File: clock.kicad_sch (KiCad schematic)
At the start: 51 parts, among them J1 USB_C_Receptacle_USB2.0_16P, J2 Conn_01x02_Pin, J3 Conn_01x02_Pin, J4 Conn_01x02_Pin, J5 Battery, Q1 2N7002K, Q2 NPN, SW1 SW_Push, SW2 SW_Push, SW3 SW_Push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

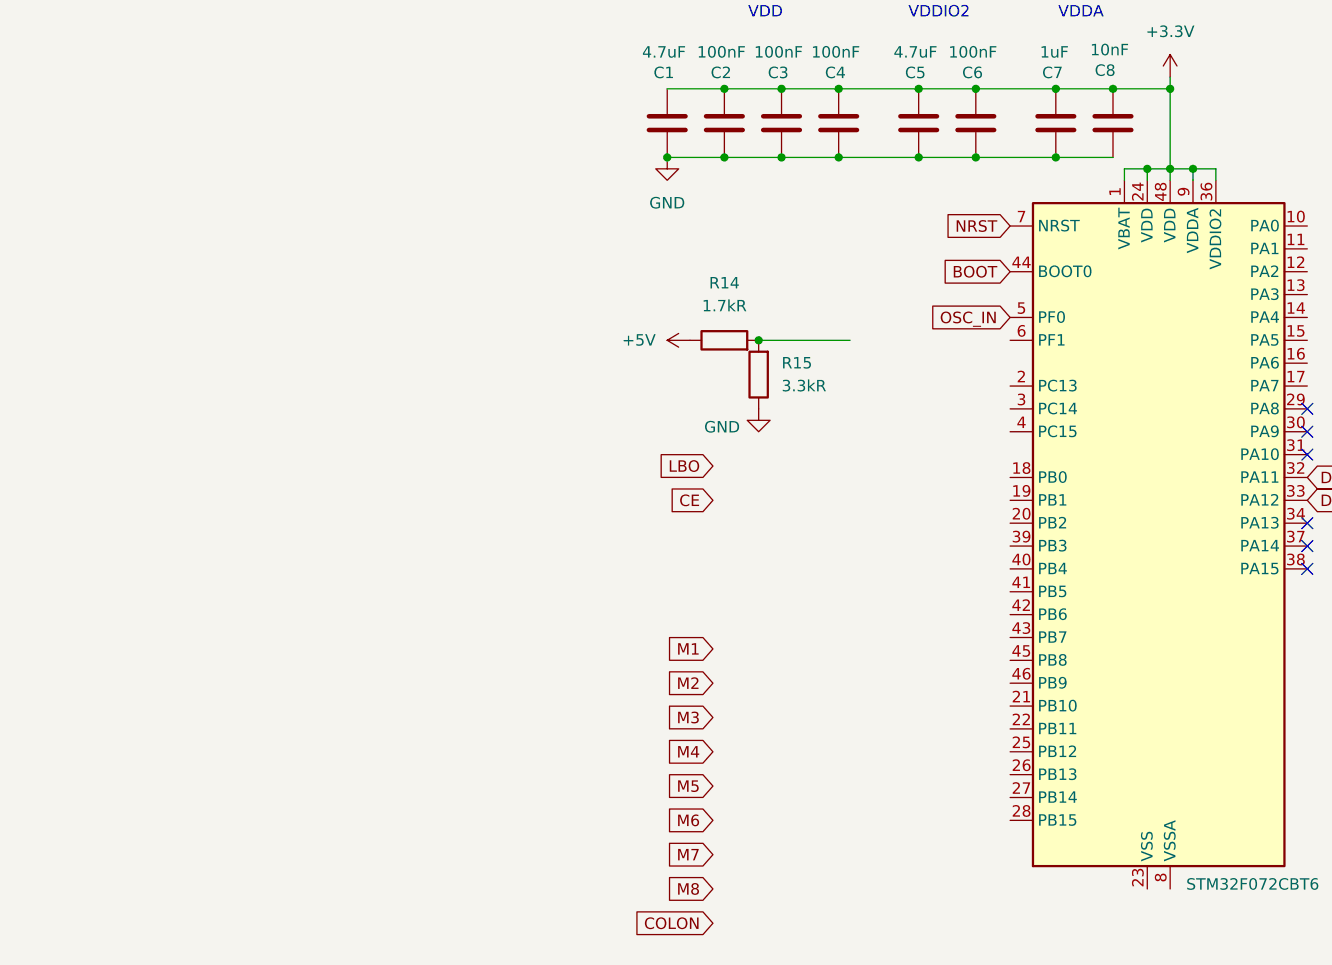
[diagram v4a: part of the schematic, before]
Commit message: actually grounded STM, changed charlie plexed resistors, added note for charging logic, added switch for the 5V logic detection
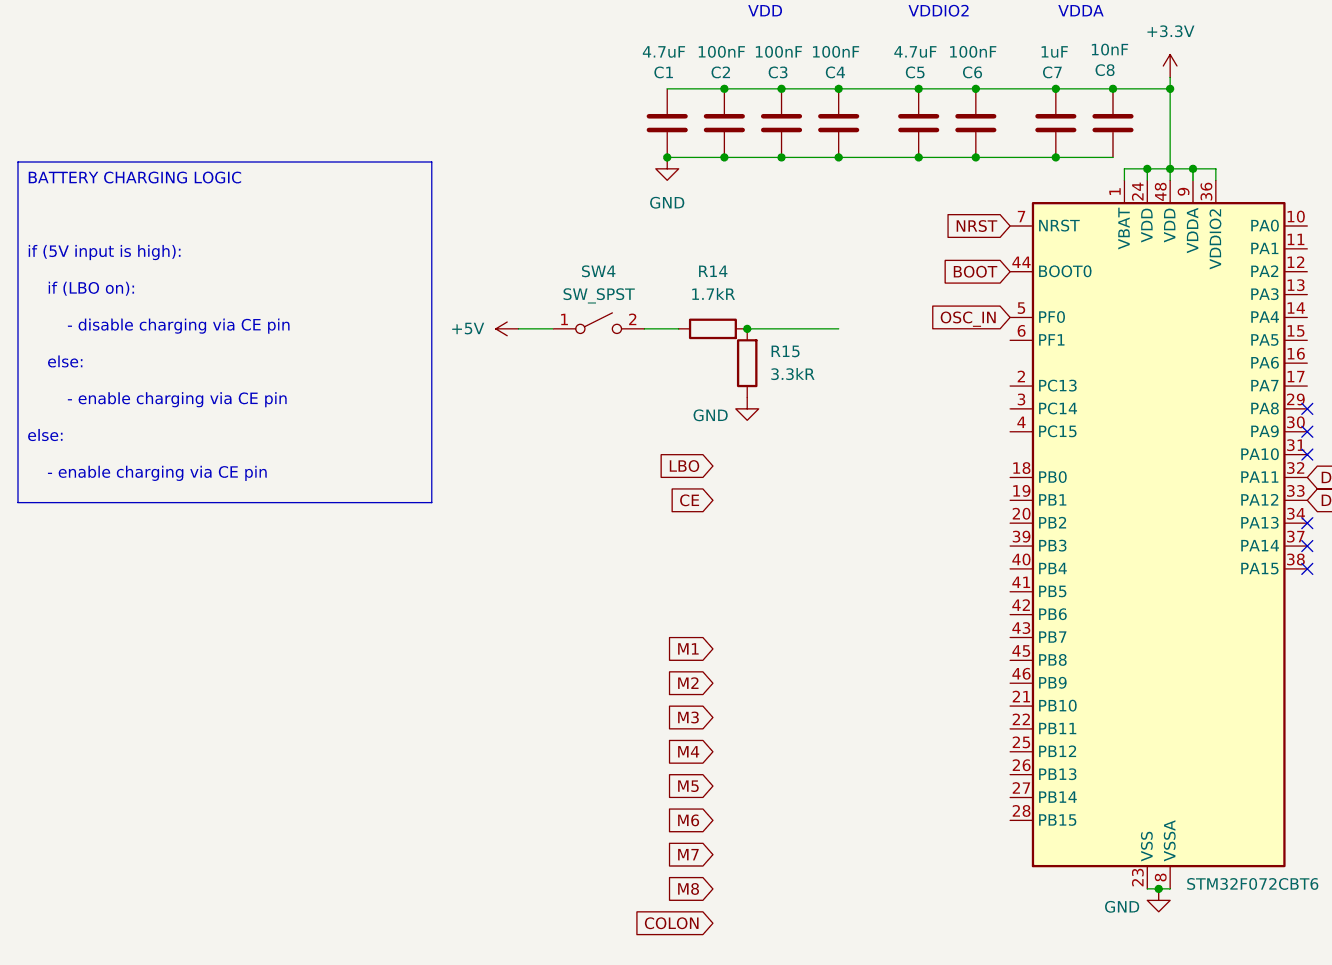
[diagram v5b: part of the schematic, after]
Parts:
- added SW4: SW_SPST, symbol Switch:SW_SPST
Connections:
- net +5V: now also SW4.1 (A); no longer R14.1
- net GND: now also U1.23 (VSS), U1.35 (VSS), U1.47 (VSS), U1.8 (VSSA)
- new net: R14.1, SW4.2 (B)
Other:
- moved on the sheet: R14, R15
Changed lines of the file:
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@@
 	)
 	(junction
+		(at 71.12 189.23)
+		(diameter 0)
+		(color 0 0 0 0)
+	)
+	(junction
 		(at 35.56 107.95)
 		(diameter 0)
@@
 	)
 	(junction
-		(at 26.67 128.27)
+		(at 25.4 127)
 		(diameter 0)
 		(color 0 0 0 0)
@@
 	(wire
 		(pts
-			(xy 26.67 128.27) (xy 36.83 128.27)
+			(xy 25.4 127) (xy 35.56 127)
+		)
+		(stroke
+			(width 0)
+			(type default)
+		)
+	)
+	(wire
+		(pts
+			(xy 71.12 189.23) (xy 72.39 189.23)
 		)
 		(stroke
@@
 	(wire
 		(pts
+			(xy 69.85 189.23) (xy 71.12 189.23)
+		)
+		(stroke
+			(width 0)
+			(type default)
+		)
+	)
+	(wire
+		(pts
+			(xy 3.81 127) (xy 0 127)
+		)
+		(stroke
+			(width 0)
+			(type default)
+		)
+	)
+	(wire
+		(pts
 			(xy 153.67 107.95) (xy 168.91 107.95)
 		)
@@
 	(wire
 		(pts
+			(xy 17.78 127) (xy 13.97 127)
+		)
+		(stroke
+			(width 0)
+			(type default)
+		)
+	)
+	(wire
+		(pts
 			(xy 153.67 90.17) (xy 158.75 90.17)
 		)
@@
 		)
 	)
+	(text_box "BATTERY CHARGING LOGIC\n\n\n\nif (5V input is high):\n\n	if (LBO on):\n		\n		- disable charging via CE pin\n\n	else:\n		\n		- enable charging via CE pin\n\nelse:\n\n	- enable charging via CE pin\n"
+		(exclude_from_sim no)
+		(at -55.626 108.458 0)
+		(size 45.974 37.846)
+		(stroke
+			(width 0)
+			(type default)
+		)
+		(fill
+			(type none)
+		)
+		(effects
+			(font
+				(size 1.27 1.27)
+			)
+			(justify left top)
+		)
+	)
 	(text_box "\"It is recommended to use X7R or X5R dielectric capacitor if 1.0µF ceramic capacitor is selected as input/output capacitors.\""
 		(exclude_from_sim no)
@@
 	(symbol
 		(lib_id "Device:R")
-		(at 22.86 128.27 90)
+		(at 21.59 127 90)
 		(unit 1)
 		(exclude_from_sim no)
@@
 		(fields_autoplaced yes)
 		(property "Reference" "R14"
-			(at 22.86 121.92 90)
+			(at 21.59 120.65 90)
 			(effects
 				(font
@@
 		)
 		(property "Value" "1.7kR"
-			(at 22.86 124.46 90)
+			(at 21.59 123.19 90)
 			(effects
 				(font
@@
 		)
 		(property "Footprint" ""
-			(at 22.86 130.048 90)
+			(at 21.59 128.778 90)
 			(effects
 				(font
@@
 		)
 		(property "Datasheet" "~"
-			(at 22.86 128.27 0)
+			(at 21.59 127 0)
 			(effects
 				(font
@@
 		)
 		(property "Description" "Resistor"
-			(at 22.86 128.27 0)
+			(at 21.59 127 0)
 			(effects
 				(font
@@
 	)
 	(symbol
+		(lib_id "Switch:SW_SPST")
+		(at 8.89 127 0)
+		(unit 1)
+		(exclude_from_sim no)
+		(in_bom yes)
+		(on_board yes)
+		(dnp no)
+		(fields_autoplaced yes)
+		(property "Reference" "SW4"
+			(at 8.89 120.65 0)
+			(effects
+				(font
+					(size 1.27 1.27)
+				)
+			)
+		)
+		(property "Value" "SW_SPST"
+			(at 8.89 123.19 0)
+			(effects
+				(font
+					(size 1.27 1.27)
+				)
+			)
+		)
+		(property "Footprint" ""
+			(at 8.89 127 0)
+			(effects
+				(font
+					(size 1.27 1.27)
+				)
+				(hide yes)
+			)
+		)
+		(property "Datasheet" "~"
+			(at 8.89 127 0)
+			(effects
+				(font
+					(size 1.27 1.27)
+				)
+				(hide yes)
+			)
+		)
+		(property "Description" "Single Pole Single Throw (SPST) switch"
+			(at 8.89 127 0)
+			(effects
+				(font
+					(size 1.27 1.27)
+				)
+				(hide yes)
+			)
+		)
+		(pin "1"
+		)
+		(pin "2"
+		)
+		(instances
+			(project "clock"
+				(path "/959d2641-02eb-4caa-b1c6-84a86321825f"
+					(reference "SW4")
+					(unit 1)
+				)
+			)
+		)
+	)
+	(symbol
 		(lib_id "Device:R")
 		(at 105.41 82.55 90)
@@
 	(symbol
 		(lib_id "power:GND")
+		(at 71.12 189.23 0)
+		(unit 1)
+		(exclude_from_sim no)
+		(in_bom yes)
+		(on_board yes)
+		(dnp no)
+		(property "Reference" "#PWR038"
+			(at 71.12 195.58 0)
+			(effects
+				(font
+					(size 1.27 1.27)
+				)
+				(hide yes)
+			)
+		)
+		(property "Value" "GND"
+			(at 67.056 191.262 0)
+			(effects
+				(font
+					(size 1.27 1.27)
+				)
+			)
+		)
+		(property "Footprint" ""
+			(at 71.12 189.23 0)
+			(effects
+				(font
+					(size 1.27 1.27)
+				)
+				(hide yes)
+			)
+		)
+		(property "Datasheet" ""
+			(at 71.12 189.23 0)
+			(effects
+				(font
+					(size 1.27 1.27)
+				)
+				(hide yes)
+			)
+		)
+		(property "Description" "Power symbol creates a global label with name \"GND\" , ground"
+			(at 71.12 189.23 0)
+			(effects
+				(font
+					(size 1.27 1.27)
+				)
+				(hide yes)
+			)
+		)
+		(pin "1"
+		)
+		(instances
+			(project "clock"
+				(path "/959d2641-02eb-4caa-b1c6-84a86321825f"
+					(reference "#PWR038")
+					(unit 1)
+				)
+			)
+		)
+	)
+	(symbol
+		(lib_id "power:GND")
 		(at 123.19 40.64 0)
 		(unit 1)
@@
 	(symbol
 		(lib_id "power:+5V")
-		(at 19.05 128.27 90)
+		(at 0 127 90)
 		(unit 1)
 		(exclude_from_sim no)
@@
 		(fields_autoplaced yes)
 		(property "Reference" "#PWR021"
-			(at 22.86 128.27 0)
+			(at 3.81 127 0)
 			(effects
 				(font
@@
 		)
 		(property "Value" "+5V"
-			(at 15.24 128.2699 90)
+			(at -3.81 126.9999 90)
 			(effects
 				(font
@@
 		)
 		(property "Footprint" ""
-			(at 19.05 128.27 0)
+			(at 0 127 0)
 			(effects
 				(font
@@
 		)
 		(property "Datasheet" ""
-			(at 19.05 128.27 0)
+			(at 0 127 0)
 			(effects
 				(font
@@
 		)
 		(property "Description" "Power symbol creates a global label with name \"+5V\""
-			(at 19.05 128.27 0)
+			(at 0 127 0)
 			(effects
 				(font
@@
 	(symbol
 		(lib_id "Device:R")
-		(at 26.67 132.08 180)
+		(at 25.4 130.81 180)
 		(unit 1)
 		(exclude_from_sim no)
@@
 		(fields_autoplaced yes)
 		(property "Reference" "R15"
-			(at 29.21 130.8099 0)
+			(at 27.94 129.5399 0)
 			(effects
 				(font
@@
 		)
 		(property "Value" "3.3kR"
-			(at 29.21 133.3499 0)
+			(at 27.94 132.0799 0)
 			(effects
 				(font
@@
 		)
 		(property "Footprint" ""
-			(at 28.448 132.08 90)
+			(at 27.178 130.81 90)
 			(effects
 				(font
@@
 		)
 		(property "Datasheet" "~"
-			(at 26.67 132.08 0)
+			(at 25.4 130.81 0)
 			(effects
 				(font
@@
 		)
 		(property "Description" "Resistor"
-			(at 26.67 132.08 0)
+			(at 25.4 130.81 0)
 			(effects
 				(font
@@
 	(symbol
 		(lib_id "power:GND")
-		(at 26.67 135.89 0)
+		(at 25.4 134.62 0)
 		(unit 1)
 		(exclude_from_sim no)
@@
 		(dnp no)
 		(property "Reference" "#PWR035"
-			(at 26.67 142.24 0)
+			(at 25.4 140.97 0)
 			(effects
 				(font
@@
 		)
 		(property "Value" "GND"
-			(at 22.606 137.922 0)
+			(at 21.336 136.652 0)
 			(effects
 				(font
@@
 		)
 		(property "Footprint" ""
-			(at 26.67 135.89 0)
+			(at 25.4 134.62 0)
 			(effects
 				(font
@@
 		)
 		(property "Datasheet" ""
-			(at 26.67 135.89 0)
+			(at 25.4 134.62 0)
 			(effects
 				(font
@@
 		)
 		(property "Description" "Power symbol creates a global label with name \"GND\" , ground"
-			(at 26.67 135.89 0)
+			(at 25.4 134.62 0)
 			(effects
 				(font

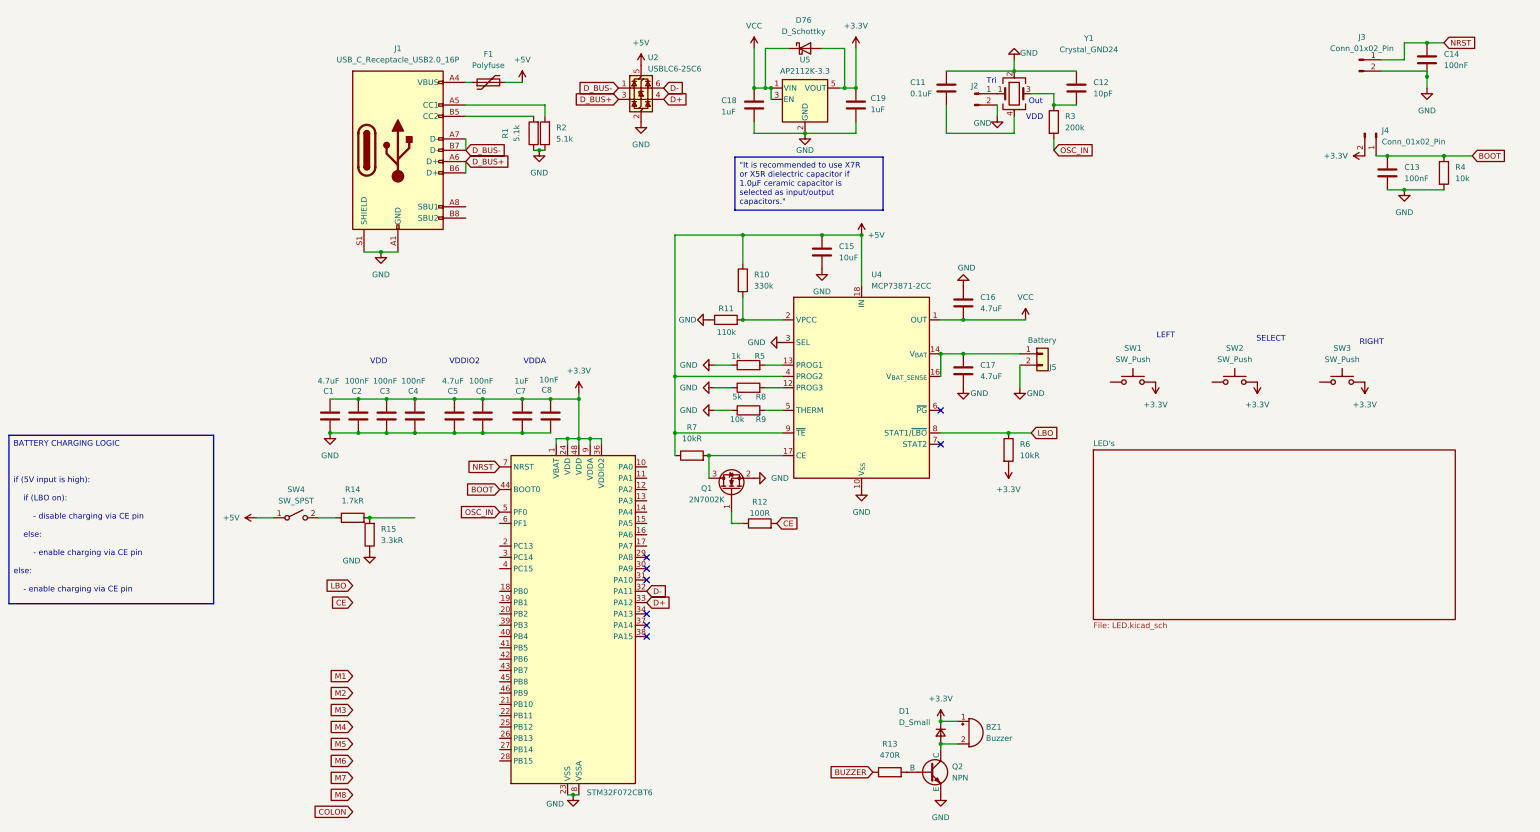
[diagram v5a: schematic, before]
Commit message: added lables for buttons
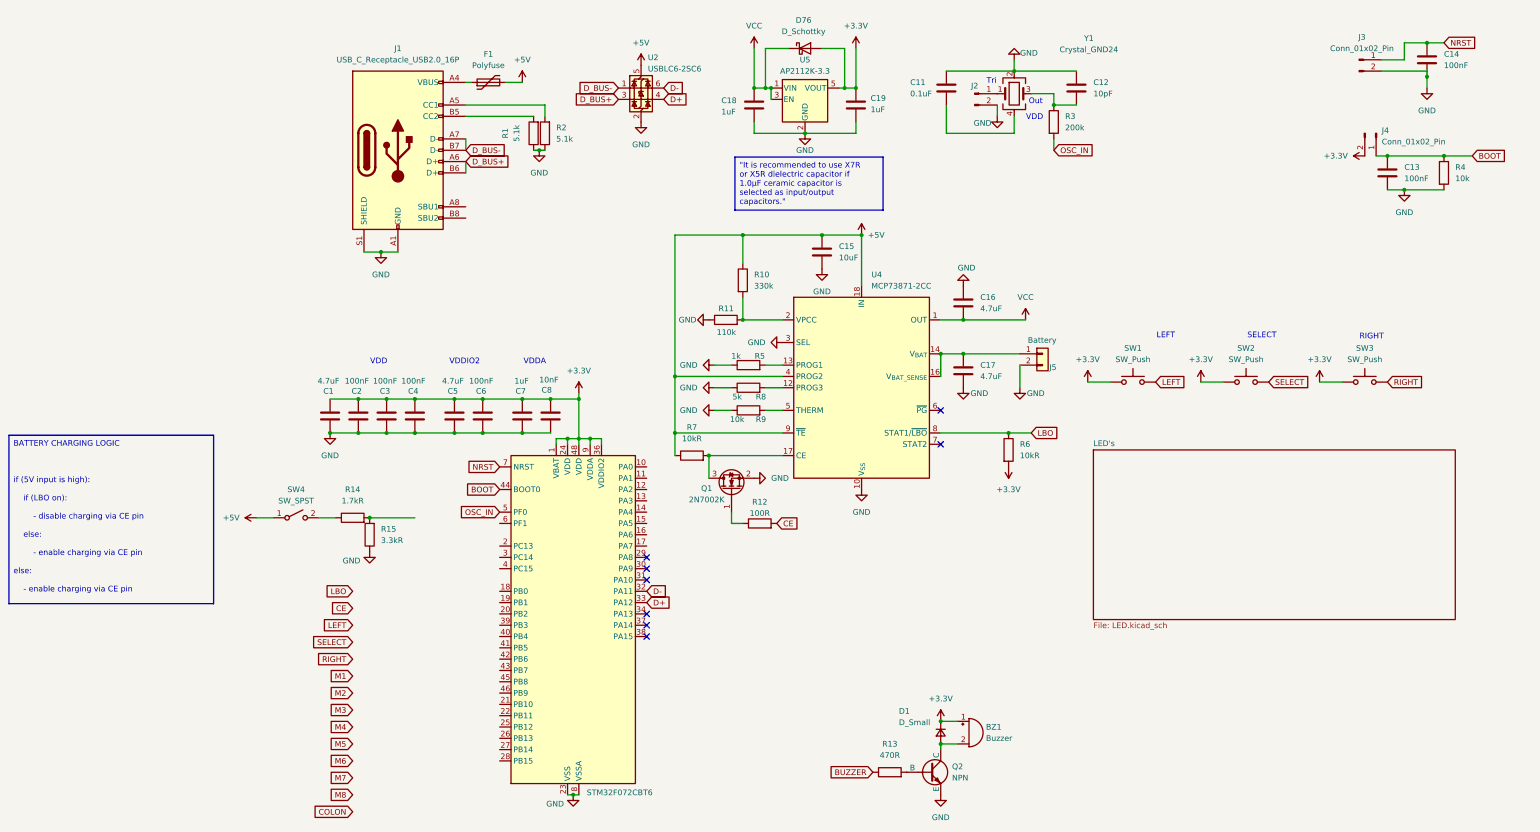
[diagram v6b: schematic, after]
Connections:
- net +3.3V: now also SW1.1, SW2.1, SW3.1; no longer SW1.2, SW2.2, SW3.2
- new net LEFT: SW1.2
- new net RIGHT: SW3.2
- new net SELECT: SW2.2

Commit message: done loads, added indication LED, changed how switches works, added footprints for lots of things, set up editor for laying things out
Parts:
- added D74: LED, LED_SMD:LED_0603_1608Metric_Pad1.05x0.95mm_HandSolder, symbol Device:LED
- added R31: 300R, Resistor_SMD:R_0402_1005Metric_Pad0.72x0.64mm_HandSolder, symbol Device:R
- BZ1: footprint (none) -> Buzzer_Beeper:MagneticBuzzer_CUI_CMT-8504-100-SMT
- J1: footprint (none) -> Connector_USB:USB_C_Receptacle_Palconn_UTC16-G
- Q2: footprint (none) -> Package_TO_SOT_SMD:SOT-23_Handsoldering
- R10, R11, R3: footprint (none) -> Resistor_SMD:R_0603_1608Metric_Pad0.98x0.95mm_HandSolder
- R12, R13, R6, R7: footprint (none) -> Resistor_SMD:R_0402_1005Metric_Pad0.72x0.64mm_HandSolder
- R14: value 1.7kR -> 1kR; footprint (none) -> Resistor_SMD:R_0402_1005Metric_Pad0.72x0.64mm_HandSolder
- R15: value 3.3kR -> 2kR; footprint (none) -> Resistor_SMD:R_0402_1005Metric_Pad0.72x0.64mm_HandSolder
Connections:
- net +3.3V: no longer SW1.1, SW2.1, SW3.1
- net GND: now also SW1.1, SW2.1, SW3.1, D74.1 (K)
- net at R14.1, SW4.2 (B): now also R31.1
- net 5V_TEST: now reaches R14.2, R15.2
- new net: D74.2 (A), R31.2
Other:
- moved on the sheet: BZ1, C13, D1, J4, Q2, R13, R4, SW1, SW2, SW3
